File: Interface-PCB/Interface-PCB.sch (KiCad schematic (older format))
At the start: 43 parts, among them IC1 SN74LVC245AN, J1 BARREL_JACK_PAD, J10 CONN_05JST-VERT, J11 TEMPERATURE_SENSOR, J12 CONN_05JST-VERT, J13 I2C_HEADER, J2 BARREL_JACK_PAD, J3 LEVEL_SENSOR, J4 RASPBERRYPI-40-PIN-GPIO, J5 LEVEL_SENSOR, J6 LEVEL_SENSOR, J7 LEVEL_SENSOR, J9 TEMPERATURE_SENSOR, M1 PERISTALTIC_PUMP, M2 PERISTALTIC_PUMP, M3 PERISTALTIC_PUMP, Q1 2N3904, Q10 2N3904, Q2 2N3904, Q3 2N3904, Q4 2N3904, Q5 2N3904, Q6 2N3904, Q7 2N3904, Q8 2N3904, Q9 2N3904, U1 TB6612FNG_BREAKOUT, U2 TB6612FNG_BREAKOUT

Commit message: Split schematic sheets
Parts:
- removed J10, J12: CONN_05JST-VERT, JST-5-PTH-VERT, symbol SparkFun-Connectors:CONN_05JST-VERT
- removed J11, J9: TEMPERATURE_SENSOR, Connector_JST:JST_XH_B3B-XH-A_1x03_P2.50mm_Vertical, symbol AA_Custom_Components:TEMPERATURE_SENSOR
- removed J3, J5, J6, J7, J? (x2): LEVEL_SENSOR, Connector_JST:JST_XH_B3B-XH-A_1x03_P2.50mm_Vertical, symbol AA_Custom_Components:LEVEL_SENSOR
- removed Q1, Q10, Q2, Q3, Q4, Q5, Q6, Q7, Q8, Q9: 2N3904, Package_TO_SOT_THT:TO-92_Inline, symbol Transistor_BJT:2N3904
- removed R1, R10, R11, R12, R2, R3, R4, R5, R8, R9: 680, symbol Device:R
- removed R6: 4.7k, symbol Device:R
- removed R7: 10k, symbol Device:R
- removed U?: CD74HC4067_MUX, digikey-footprints:SOIC-24_W7.50mm, symbol AA_Custom_Components:CD74HC4067_MUX
- renumbered J4 to J3, J13 to J4
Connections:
- net labels removed: FLOW_3V3, OUTLET_1_OFF, OUTLET_1_ON, OUTLET_2_OFF, OUTLET_2_ON, OUTLET_3_OFF, OUTLET_3_ON, OUTLET_4_OFF, OUTLET_4_ON, OUTLET_5_OFF, OUTLET_5_ON, OUT_1_OFF, OUT_1_ON, OUT_2_OFF, OUT_2_ON, OUT_3_OFF, OUT_3_ON, OUT_4_OFF, OUT_4_ON, OUT_5_OFF, OUT_5_ON
- wire segments 117 -> 100
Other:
- note added: "ENVIRONMENTAL SENSORS"
- note removed: "DHT11 - Air Temperature \n and Humidity"
- note removed: "DS18B20 - Water Temperature"
- note removed: "Do not populate 10k"
- note removed: "ENVIRONMENT SENSORS"
- note removed: "Nutrient Level"
- note removed: "RADIO TRANSMITTER CONTROL"
- note removed: "TODO: mux Transistor outputs"
- note removed: "Water Flow"
- note removed: "Water Level"
- note removed: "Water Level - Bottom Tray"
- note removed: "Water Level - Top Tray"
- note removed: "pH Down Level"
- note removed: "pH Up Level"
- moved on the sheet: IC1, J1, J2, J3, J4, M3, U2

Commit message: Assign misc footprints for FDP
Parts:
- IC1: footprint digikey-footprints:DIP-20_W7.62mm -> Package_DIP:DIP-20_W7.62mm_LongPads
- J1, J2, M1, M2, M3: footprint (none) -> Fuses:1206
- J4: footprint Connector_JST:JST_XH_B4B-XH-AM_1x04_P2.50mm_Vertical -> Connector_JST:JST_XH_B4B-XH-A_1x04_P2.50mm_Vertical
- U1, U2: footprint (none) -> Package_DIP:DIP-16_W7.62mm_LongPads
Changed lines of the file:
@@
 F 0 "IC1" H 2450 1265 50  0000 C CNN
 F 1 "SN74LVC245AN" H 2450 1174 50  0000 C CNN
-F 2 "digikey-footprints:DIP-20_W7.62mm" H 2800 1100 50  0001 L CNN
+F 2 "Package_DIP:DIP-20_W7.62mm_LongPads" H 2800 1100 50  0001 L CNN
 F 3 "http://www.ti.com/lit/gpn/sn74hct245" H 2800 1000 50  0001 L CNN
 F 4 "Octal Bus Transceivers With 3-State Outputs" H 2800 900 50  0001 L CNN "Description"
@@
 F 0 "U1" H 2150 7167 50  0000 C CNN
 F 1 "TB6612FNG_BREAKOUT" H 2150 7076 50  0000 C CNN
-F 2 "" H 1600 6800 50  0001 L CNN
+F 2 "Package_DIP:DIP-16_W7.62mm_LongPads" H 1600 6800 50  0001 L CNN
 F 3 "" H 2300 6800 50  0001 C CNN
 	1    2150 6550
@@
 F 0 "M1" H 1108 7054 45  0000 C CNN
 F 1 "PERISTALTIC_PUMP" H 1108 6970 45  0000 C CNN
-F 2 "" H 1300 7100 20  0001 C CNN
+F 2 "Fuses:1206" H 1300 7100 20  0001 C CNN
 F 3 "" H 1300 6650 50  0001 C CNN
 	1    1050 6650
@@
 F 0 "M2" H 1108 7754 45  0000 C CNN
 F 1 "PERISTALTIC_PUMP" H 1108 7670 45  0000 C CNN
-F 2 "" H 1300 7800 20  0001 C CNN
+F 2 "Fuses:1206" H 1300 7800 20  0001 C CNN
 F 3 "" H 1300 7350 50  0001 C CNN
 	1    1050 7350
@@
 F 0 "U2" H 4800 7167 50  0000 C CNN
 F 1 "TB6612FNG_BREAKOUT" H 4800 7076 50  0000 C CNN
-F 2 "" H 4250 6800 50  0001 L CNN
+F 2 "Package_DIP:DIP-16_W7.62mm_LongPads" H 4250 6800 50  0001 L CNN
 F 3 "" H 4950 6800 50  0001 C CNN
 	1    4800 6550
@@
 F 0 "M3" H 3858 7054 45  0000 C CNN
 F 1 "PERISTALTIC_PUMP" H 3858 6970 45  0000 C CNN
-F 2 "" H 4050 7100 20  0001 C CNN
+F 2 "Fuses:1206" H 4050 7100 20  0001 C CNN
 F 3 "" H 4050 6650 50  0001 C CNN
 	1    3800 6650
@@
 F 0 "J1" H 1807 3575 50  0000 C CNN
 F 1 "BARREL_JACK_PAD" H 1807 3484 50  0000 C CNN
-F 2 "" H 1800 3210 50  0001 C CNN
+F 2 "Fuses:1206" H 1800 3210 50  0001 C CNN
 F 3 "~" H 1800 3210 50  0001 C CNN
 	1    1750 3250
@@
 F 0 "J2" H 1857 4575 50  0000 C CNN
 F 1 "BARREL_JACK_PAD" H 1857 4484 50  0000 C CNN
-F 2 "" H 1850 4210 50  0001 C CNN
+F 2 "Fuses:1206" H 1850 4210 50  0001 C CNN
 F 3 "~" H 1850 4210 50  0001 C CNN
 	1    1800 4250
@@
 F 0 "J4" H 8058 5104 45  0000 C CNN
 F 1 "I2C_HEADER" H 8058 5020 45  0000 C CNN
-F 2 "Connector_JST:JST_XH_B4B-XH-AM_1x04_P2.50mm_Vertical" H 8100 5100 20  0001 C CNN
+F 2 "Connector_JST:JST_XH_B4B-XH-A_1x04_P2.50mm_Vertical" H 8100 5100 20  0001 C CNN
 F 3 "" H 8100 4700 50  0001 C CNN
 	1    8100 4700

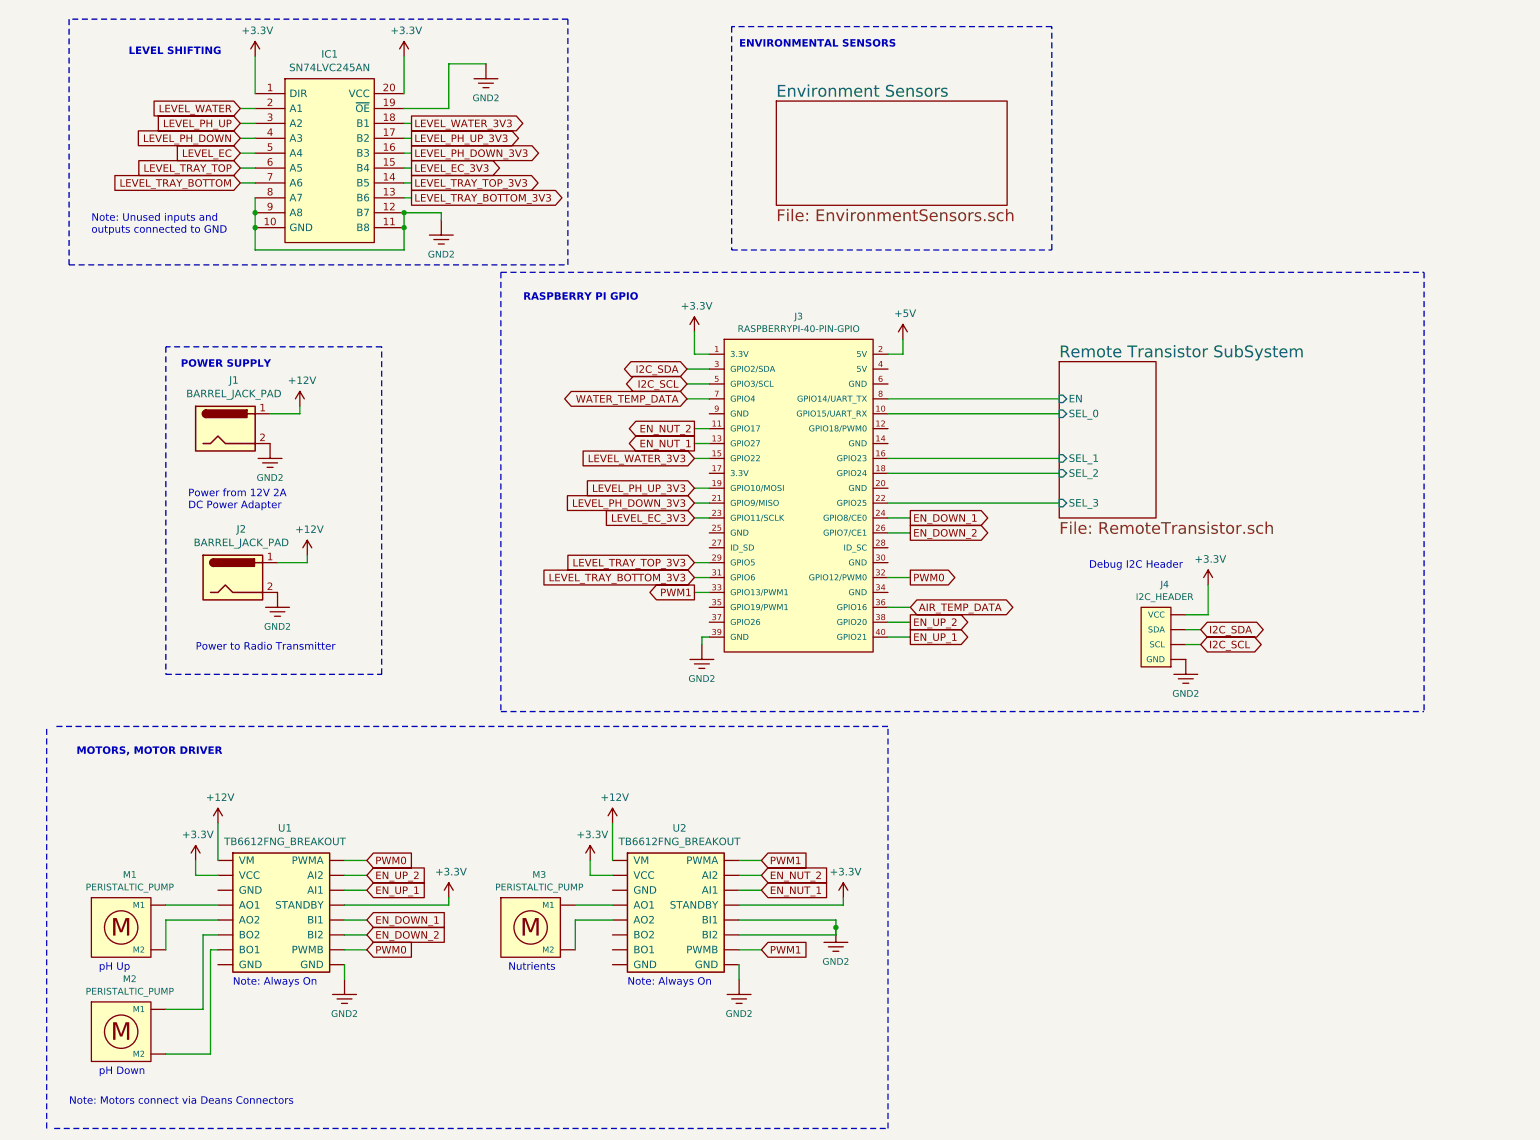
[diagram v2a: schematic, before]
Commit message: Add diagrams and datasheets
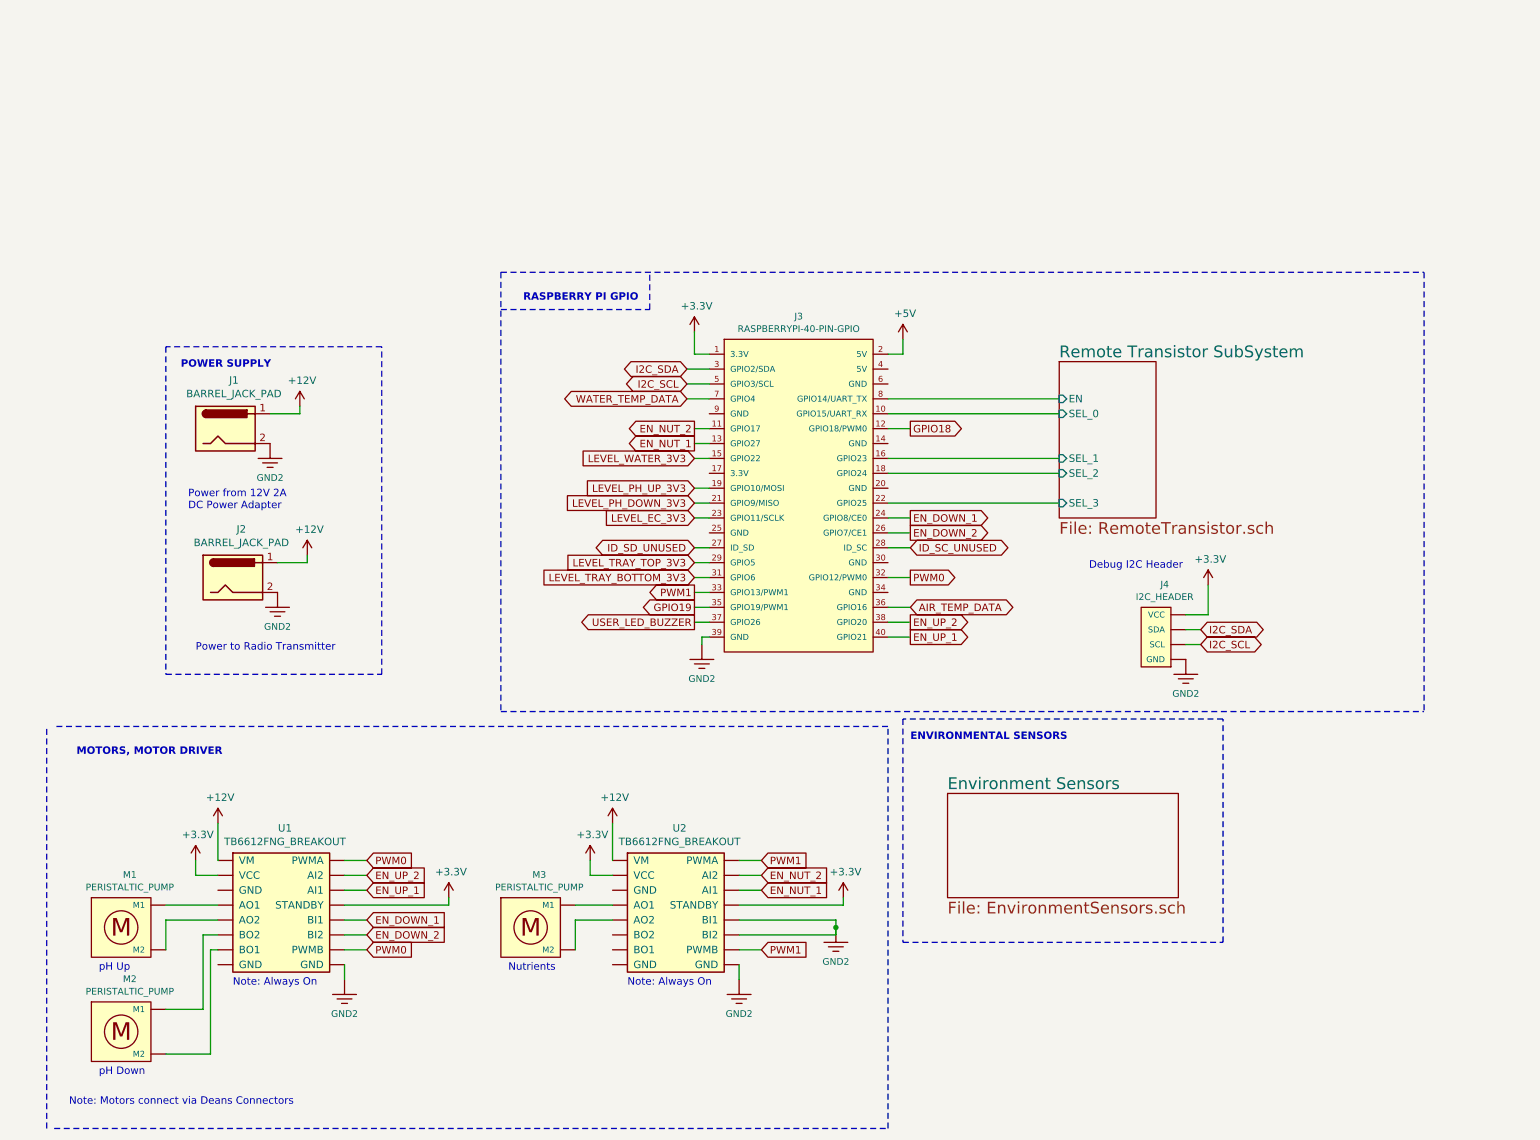
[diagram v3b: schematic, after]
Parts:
- removed IC1: SN74LVC245AN, Package_DIP:DIP-20_W7.62mm_LongPads, symbol AA_Custom_Components:SN74LVC245AN
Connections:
- net GPIO18: now reaches J3.12 (GPIO18/PWM0)
- net ID_SD_UNUSED: now reaches J3.27 (ID_SD)
- net ID_SC_UNUSED: now reaches J3.28 (ID_SC)
- net GPIO19: now reaches J3.35 (GPIO19/PWM1)
- net USER_LED_BUZZER: now reaches J3.37 (GPIO26)
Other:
- note removed: "LEVEL SHIFTING"
- note removed: "Note: Unused inputs and \noutputs connected to GND"
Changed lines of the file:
@@
 $EndDescr
-$Comp
-L SparkFun-PowerSymbols:GND2 #GND05
-U 1 1 61A1C0EA
-P 3500 800
-F 0 "#GND05" H 3550 750 45  0001 L BNN
-F 1 "GND2" H 3500 570 45  0000 C CNN
-F 2 "" H 3500 475 60  0000 C CNN
-F 3 "" H 3500 700 60  0001 C CNN
-	1    3500 800
-	1    0    0    -1
-$EndComp
 $Comp
 L power:+12V #PWR02
@@
 	1    0    0    -1
 $EndComp
-$Comp
-L SparkFun-PowerSymbols:GND2 #GND04
-U 1 1 61A1B44E
-P 3200 1850
-F 0 "#GND04" H 3250 1800 45  0001 L BNN
-F 1 "GND2" H 3200 1620 45  0000 C CNN
-F 2 "" H 3200 1525 60  0000 C CNN
-F 3 "" H 3200 1750 60  0001 C CNN
-	1    3200 1850
-	1    0    0    -1
-$EndComp
-Text Notes 850  1950 0    50   ~ 0
-Note: Unused inputs and \noutputs connected to GND
-Text GLabel 1850 1100 0    50   Input ~ 0
-LEVEL_WATER
-Wire Wire Line
-	1850 1100 1950 1100
-Text GLabel 1850 1200 0    50   Input ~ 0
-LEVEL_PH_UP
-Text GLabel 1850 1300 0    50   Input ~ 0
-LEVEL_PH_DOWN
-Text GLabel 1850 1400 0    50   Input ~ 0
-LEVEL_EC
-Wire Wire Line
-	1850 1200 1950 1200
-Wire Wire Line
-	1850 1300 1950 1300
-Wire Wire Line
-	1850 1400 1950 1400
-Text GLabel 3000 1500 2    50   Output ~ 0
-LEVEL_EC_3V3
-Wire Wire Line
-	2950 1100 3250 1100
-Wire Wire Line
-	3250 1100 3250 800
-Wire Wire Line
-	3250 800  3500 800
 Wire Notes Line
 	6200 7950 6200 5250
@@
 	1350 2700 1350 4900
 Wire Wire Line
-	2950 1000 2950 750
-Wire Wire Line
-	1950 1000 1950 750
-$Comp
-L AA_Custom_Components:SN74LVC245AN IC1
-U 1 1 6378BCA1
-P 1950 1000
-F 0 "IC1" H 2450 1265 50  0000 C CNN
-F 1 "SN74LVC245AN" H 2450 1174 50  0000 C CNN
-F 2 "Package_DIP:DIP-20_W7.62mm_LongPads" H 2800 1100 50  0001 L CNN
-F 3 "http://www.ti.com/lit/gpn/sn74hct245" H 2800 1000 50  0001 L CNN
-F 4 "Octal Bus Transceivers With 3-State Outputs" H 2800 900 50  0001 L CNN "Description"
-F 5 "5.08" H 2800 800 50  0001 L CNN "Height"
-F 6 "Texas Instruments" H 2800 700 50  0001 L CNN "Manufacturer_Name"
-F 7 "296-8503-5-ND" H 2800 600 50  0001 L CNN "Manufacturer_Part_Number"
-	1    1950 1000
-	1    0    0    -1
-$EndComp
-Wire Wire Line
-	2950 1800 2950 1900
-Wire Wire Line
-	1950 1700 1950 1800
-Wire Wire Line
-	1950 1900 1950 2050
-Wire Wire Line
-	1950 1900 1950 1800
-Connection ~ 1950 1900
-Connection ~ 1950 1800
-Wire Wire Line
-	2950 1900 2950 2050
-Wire Wire Line
-	2950 2050 1950 2050
-Connection ~ 2950 1900
-$Comp
-L power:+3.3V #PWR06
-U 1 1 6383D4F5
-P 2950 750
-F 0 "#PWR06" H 2950 600 50  0001 C CNN
-F 1 "+3.3V" H 2965 923 50  0000 C CNN
-F 2 "" H 2950 750 50  0001 C CNN
-F 3 "" H 2950 750 50  0001 C CNN
-	1    2950 750
-	1    0    0    -1
-$EndComp
-$Comp
-L power:+3.3V #PWR03
-U 1 1 6385FC22
-P 1950 750
-F 0 "#PWR03" H 1950 600 50  0001 C CNN
-F 1 "+3.3V" H 1965 923 50  0000 C CNN
-F 2 "" H 1950 750 50  0001 C CNN
-F 3 "" H 1950 750 50  0001 C CNN
-	1    1950 750
-	1    0    0    -1
-$EndComp
-Text GLabel 3000 1300 2    50   Output ~ 0
-LEVEL_PH_UP_3V3
-Text GLabel 3000 1200 2    50   Output ~ 0
-LEVEL_WATER_3V3
-Wire Wire Line
 	2700 6150 2550 6150
 Wire Wire Line
@@
 Wire Wire Line
 	2700 6750 2550 6750
-Text GLabel 3000 1400 2    50   Output ~ 0
-LEVEL_PH_DOWN_3V3
 Text GLabel 2700 6650 2    50   Input ~ 0
 EN_DOWN_2
@@
 Text Notes 1550 4750 0    50   ~ 0
 Power to Radio Transmitter
-Text Notes 1100 750  0    50   ~ 10
-LEVEL SHIFTING
-Wire Wire Line
-	2950 1200 3000 1200
-Wire Wire Line
-	2950 1300 3000 1300
-Wire Wire Line
-	2950 1400 3000 1400
-Wire Wire Line
-	2950 1500 3000 1500
-Wire Wire Line
-	2950 1600 3000 1600
 Text GLabel 4900 3850 0    50   Input ~ 0
 LEVEL_EC_3V3
@@
 Wire Wire Line
 	6200 4450 6350 4450
-Text GLabel 1850 1500 0    50   Input ~ 0
-LEVEL_TRAY_TOP
-Text GLabel 1850 1600 0    50   Input ~ 0
-LEVEL_TRAY_BOTTOM
-Wire Wire Line
-	1850 1500 1950 1500
-Wire Wire Line
-	1850 1600 1950 1600
-Text GLabel 3000 1600 2    50   Output ~ 0
-LEVEL_TRAY_TOP_3V3
-Text GLabel 3000 1700 2    50   Output ~ 0
-LEVEL_TRAY_BOTTOM_3V3
-Wire Wire Line
-	2950 1700 3000 1700
 Text GLabel 4900 4250 0    50   Input ~ 0
 LEVEL_TRAY_BOTTOM_3V3
@@
 Wire Notes Line
 	3600 2200 9800 2200
-Text Notes 5200 700  0    50   ~ 10
+Text Notes 6350 5350 0    50   ~ 10
 ENVIRONMENTAL SENSORS
 $Sheet
@@
 F6 "SEL_3" I L 7350 3750 50
 $EndSheet
-Wire Wire Line
-	2950 1800 3200 1800
-Wire Wire Line
-	3200 1800 3200 1850
-Connection ~ 2950 1800
+Wire Notes Line
+	6300 6700 8450 6700
+Wire Notes Line
+	8450 6700 8450 5200
+Wire Notes Line
+	8450 5200 6300 5200
+Wire Notes Line
+	6300 5200 6300 6700
+Wire Notes Line
+	3600 2450 4600 2450
+Wire Notes Line
+	4600 2450 4600 2200
+Text GLabel 4900 4550 0    50   Output ~ 0
+USER_LED_BUZZER
+Wire Wire Line
+	4900 4550 5000 4550
+Text GLabel 4900 4450 0    50   Output ~ 0
+GPIO19
+Wire Wire Line
+	4900 4450 5000 4450
+Text GLabel 6350 4050 2    50   BiDi ~ 0
+ID_SC_UNUSED
+Text GLabel 4900 4050 0    50   BiDi ~ 0
+ID_SD_UNUSED
+Wire Wire Line
+	6350 4050 6200 4050
+Wire Wire Line
+	4900 4050 5000 4050
+Text GLabel 6350 3250 2    50   Output ~ 0
+GPIO18
+Wire Wire Line
+	6350 3250 6200 3250
 $Sheet
-S 5450 1050 1550 700
+S 6600 5700 1550 700
 U 6375997B
 F0 "Environment Sensors" 79
 F1 "EnvironmentSensors.sch" 79
 $EndSheet
-Wire Notes Line
-	5150 2050 7300 2050
-Wire Notes Line
-	7300 2050 7300 550
-Wire Notes Line
-	7300 550  5150 550
-Wire Notes Line
-	5150 550  5150 2050
-Wire Notes Line
-	700  500  700  2150
-Wire Notes Line
-	700  2150 4050 2150
-Wire Notes Line
-	4050 2150 4050 500
-Wire Notes Line
-	4050 500  700  500
 $EndSCHEMATC

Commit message: Review Schematic
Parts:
- added H1, H2, H3, H4: MountingHole, MountingHole:MountingHole_3.2mm_M3_Pad, symbol Mechanical:MountingHole
- added J3: GPIO_DEBUG_HEADER, Connector_PinHeader_2.54mm:PinHeader_2x21_P2.54mm_Vertical, symbol AA_Custom_Components:RASPBERRYPI-40-PIN-GPIO
- J4: renamed from J3; value RASPBERRYPI-40-PIN-GPIO -> RASPBERRYPI_GPIO_CONN_HEADER
- U1: footprint Package_DIP:DIP-16_W7.62mm_LongPads -> digikey-footprints:DIP-16_W7.62mm
- renumbered J4 to J5
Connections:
- net 3.3V is gone; now on net GND: J1.2, J2.2, J4.39 (GND), J5.4 (GND), U1.16 (GND), U2.13 (BI1), U2.14 (BI2), U2.16 (GND)
- net +3V3: now also J4.17 (3.3V), J3.1 (3.3V), J3.17 (3.3V)
- net +5V: now also J4.4 (5V), J3.2 (5V), J3.4 (5V)
- net AIR_TEMP_DATA: now also J3.36 (GPIO16)
- net EN_DOWN_1: now also J3.24 (GPIO8/CE0)
- net EN_DOWN_2: now also J3.26 (GPIO7/CE1)
- net EN_NUT_1: now also J3.13 (GPIO27)
- net EN_NUT_2: now also J3.11 (GPIO17)
- net EN_UP_1: now also J3.40 (GPIO21)
- net EN_UP_2: now also J3.38 (GPIO20)
- net GPIO18: now also J3.12 (GPIO18/PWM0)
- net GPIO19: now also J3.35 (GPIO19/PWM1)
- net I2C_SCL: now also J3.5 (GPIO3/SCL)
- net I2C_SDA: now also J3.3 (GPIO2/SDA)
- net ID_SC_UNUSED: now also J3.28 (ID_SC)
- net ID_SD_UNUSED: now also J3.27 (ID_SD)
- net LEVEL_EC_3V3: now also J3.23 (GPIO11/SCLK)
- net LEVEL_PH_DOWN_3V3: now also J3.21 (GPIO9/MISO)
- net LEVEL_PH_UP_3V3: now also J3.19 (GPIO10/MOSI)
- net LEVEL_TRAY_BOTTOM_3V3: now also J3.31 (GPIO6)
- net LEVEL_TRAY_TOP_3V3: now also J3.29 (GPIO5)
- net LEVEL_WATER_3V3: now also J3.15 (GPIO22)
- net PWM0: now also J3.32 (GPIO12/PWM0)
- net PWM1: now also J3.33 (GPIO13/PWM1)
- net USER_LED_BUZZER: now also J3.37 (GPIO26)
- net WATER_TEMP_DATA: now also J3.7 (GPIO4)
- net GND: now reaches J4.14 (GND)
- net GND: now also J4.20 (GND), J4.25 (GND), J4.30 (GND), J4.34 (GND), J4.6 (GND), J4.9 (GND), U1.3 (GND), U1.8 (GND), U2.3 (GND), U2.8 (GND), J3.14 (GND), J3.20 (GND), J3.25 (GND), J3.30 (GND), J3.34 (GND), J3.39 (GND), J3.6 (GND), J3.9 (GND)
- net Remote Transistor SubSystem/EN renamed MUX_EN
- net MUX_EN: now also J3.8 (GPIO14/UART_TX)
- net Remote Transistor SubSystem/SEL_0 renamed MUX_SEL0
- net MUX_SEL0: now also J3.10 (GPIO15/UART_RX)
- net Remote Transistor SubSystem/SEL_1 renamed MUX_SEL1
- net MUX_SEL1: now also J3.16 (GPIO23)
- net Remote Transistor SubSystem/SEL_2 renamed MUX_SEL2
- net MUX_SEL2: now also J3.18 (GPIO24)
- net Remote Transistor SubSystem/SEL_3 renamed MUX_SEL3
- net MUX_SEL3: now also J3.22 (GPIO25)
- no-connect marks 0 -> 2
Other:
- note added: "MOUNTING HARDWARE"
- note added: "PLANTER - INTERFACE PCB"
- note added: "REMOTE CONTROL OUTLETS"
- note added: "SPARE I2C"
- note removed: "Debug I2C Header"
- moved on the sheet: J1, J2, J4, J5, M1, M2, M3, U1, U2
